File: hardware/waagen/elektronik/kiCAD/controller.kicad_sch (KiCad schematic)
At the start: 13 parts, among them J1 AVR-ISP-6, J2 Conn_01x06, U1 ATmega1284P-P, Y1 12MHz

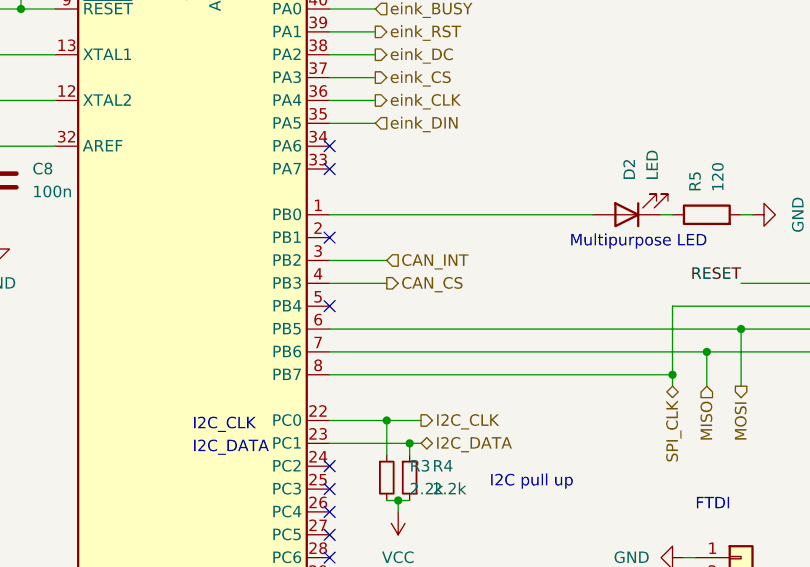
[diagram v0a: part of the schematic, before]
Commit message: CAN SPI CS pin corrected and PCB optimisations.
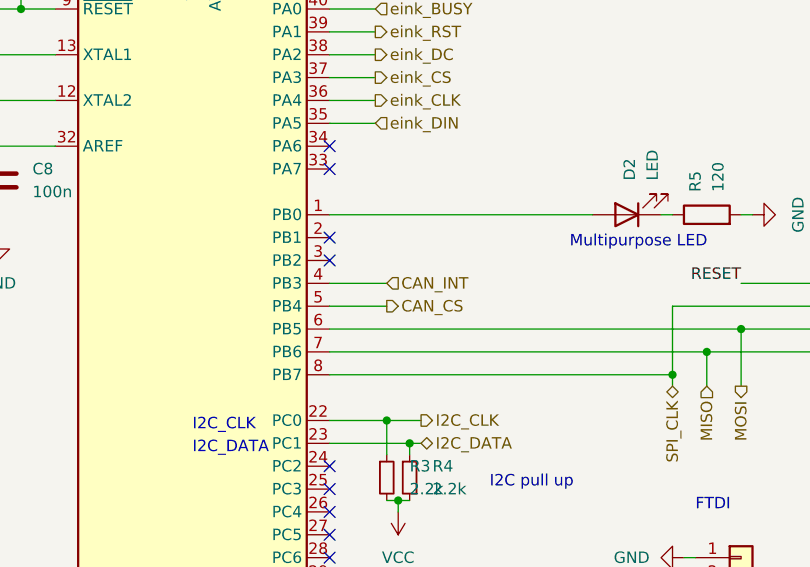
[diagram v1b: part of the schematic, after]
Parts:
- J1: footprint Connector_PinSocket_2.54mm:PinSocket_2x03_P2.54mm_Horizontal -> Connector_PinSocket_2.54mm:PinSocket_2x03_P2.54mm_Vertical
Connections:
- net CAN_CS: now also U1.5 (PB4); no longer U1.4 (PB3)
- net CAN_INT: now also U1.4 (PB3); no longer U1.3 (PB2)
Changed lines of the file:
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@@
   (no_connect (at 111.76 120.65))
   (no_connect (at 111.76 146.05))
-  (no_connect (at 111.76 95.25))
+  (no_connect (at 111.76 90.17))
   (no_connect (at 111.76 138.43))
   (no_connect (at 111.76 118.11))
@@
     (stroke (width 0) (type default) (color 0 0 0 0))
   )
-  (wire (pts (xy 111.76 90.17) (xy 118.11 90.17))
-    (stroke (width 0) (type default) (color 0 0 0 0))
-  )
   (wire (pts (xy 77.47 62.23) (xy 81.28 62.23))
     (stroke (width 0) (type default) (color 0 0 0 0))
@@
     (stroke (width 0) (type default) (color 0 0 0 0))
   )
+  (wire (pts (xy 111.76 95.25) (xy 118.11 95.25))
+    (stroke (width 0) (type default) (color 0 0 0 0))
+  )
   (wire (pts (xy 111.76 85.09) (xy 140.97 85.09))
     (stroke (width 0) (type default) (color 0 0 0 0))
   )
+  (wire (pts (xy 111.76 92.71) (xy 118.11 92.71))
+    (stroke (width 0) (type default) (color 0 0 0 0))
+  )
   (wire (pts (xy 148.59 85.09) (xy 149.86 85.09))
     (stroke (width 0) (type default) (color 0 0 0 0))
@@
   )
   (wire (pts (xy 157.48 92.71) (xy 166.37 92.71))
-    (stroke (width 0) (type default) (color 0 0 0 0))
-  )
-  (wire (pts (xy 111.76 92.71) (xy 118.11 92.71))
     (stroke (width 0) (type default) (color 0 0 0 0))
   )
@@
     (effects (font (size 1.27 1.27)) (justify right bottom))
   )
-  (hierarchical_label "CAN_INT" (shape input) (at 118.11 90.17 0)
+  (hierarchical_label "CAN_INT" (shape input) (at 118.11 92.71 0)
     (effects (font (size 1.27 1.27)) (justify left))
   )
@@
     (effects (font (size 1.27 1.27)) (justify left))
   )
-  (hierarchical_label "CAN_CS" (shape output) (at 118.11 92.71 0)
+  (hierarchical_label "CAN_CS" (shape output) (at 118.11 95.25 0)
     (effects (font (size 1.27 1.27)) (justify left))
   )
@@
       (effects (font (size 1.27 1.27)) (justify right))
     )
-    (property "Footprint" "Connector_PinSocket_2.54mm:PinSocket_2x03_P2.54mm_Horizontal" (id 2) (at 182.88 96.52 90)
-      (effects (font (size 1.27 1.27)) hide)
-    )
+    (property "Footprint" "Connector_PinSocket_2.54mm:PinSocket_2x03_P2.54mm_Vertical" (id 2) (at 182.88 96.52 90)
+      (effects (font (size 1.27 1.27)) hide)
+    )

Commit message: Error on JP1 fixed and changed scale wires pads
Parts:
- J2: footprint Connector_PinHeader_2.54mm:PinHeader_1x06_P2.54mm_Vertical -> Connector_PinSocket_2.54mm:PinSocket_1x06_P2.54mm_Vertical
- Y1: footprint Crystal:Crystal_SMD_HC49-SD -> Crystal:Crystal_SMD_HC49-SD_HandSoldering
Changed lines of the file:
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@@
       (effects (font (size 1.27 1.27)) (justify left))
     )
-    (property "Footprint" "Connector_PinHeader_2.54mm:PinHeader_1x06_P2.54mm_Vertical" (id 2) (at 157.48 128.27 0)
+    (property "Footprint" "Connector_PinSocket_2.54mm:PinSocket_1x06_P2.54mm_Vertical" (id 2) (at 157.48 128.27 0)
       (effects (font (size 1.27 1.27)) hide)
     )
@@
       (effects (font (size 1.27 1.27)) (justify right))
     )
-    (property "Footprint" "Crystal:Crystal_SMD_HC49-SD" (id 2) (at 60.96 71.12 0)
+    (property "Footprint" "Crystal:Crystal_SMD_HC49-SD_HandSoldering" (id 2) (at 60.96 71.12 0)
       (effects (font (size 1.27 1.27)) hide)
     )

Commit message: bus terminator and shelf controller added
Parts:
- J1: footprint Connector_PinSocket_2.54mm:PinSocket_2x03_P2.54mm_Vertical -> Connector_PinHeader_2.54mm:PinHeader_2x03_P2.54mm_Vertical
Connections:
- net VCC: no longer J1.2 (VCC), J2.3 (Pin_3)
- new net +9V: J1.2 (VCC), J2.3 (Pin_3)
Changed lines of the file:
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@@
     (stroke (width 0) (type default) (color 0 0 0 0))
   )
-  (wire (pts (xy 151.13 128.27) (xy 152.4 128.27))
+  (wire (pts (xy 148.59 128.27) (xy 152.4 128.27))
     (stroke (width 0) (type default) (color 0 0 0 0))
   )
@@
     (pin "1")
     (pin "2")
+  )
+  (symbol (lib_id "power:+9V") (at 179.07 110.49 180) (unit 1)
+    (in_bom yes) (on_board yes) (fields_autoplaced)
+    (property "Reference" "#PWR038" (id 0) (at 179.07 106.68 0)
+      (effects (font (size 1.27 1.27)) hide)
+    )
+    (property "Value" "+9V" (id 1) (at 179.07 115.57 0))
+    (property "Footprint" "" (id 2) (at 179.07 110.49 0)
+      (effects (font (size 1.27 1.27)) hide)
+    )
+    (property "Datasheet" "" (id 3) (at 179.07 110.49 0)
+      (effects (font (size 1.27 1.27)) hide)
+    )
+    (pin "1")
   )
   (symbol (lib_id "power:VCC") (at 119.38 118.11 180) (unit 1)
@@
     )
     (property "Datasheet" "" (id 3) (at 77.47 48.26 0)
-      (effects (font (size 1.27 1.27)) hide)
-    )
-    (pin "1")
-  )
-  (symbol (lib_id "power:VCC") (at 151.13 128.27 90) (unit 1)
-    (in_bom yes) (on_board yes) (fields_autoplaced)
-    (property "Reference" "#PWR020" (id 0) (at 154.94 128.27 0)
-      (effects (font (size 1.27 1.27)) hide)
-    )
-    (property "Value" "VCC" (id 1) (at 147.32 128.2699 90)
-      (effects (font (size 1.27 1.27)) (justify left))
-    )
-    (property "Footprint" "" (id 2) (at 151.13 128.27 0)
-      (effects (font (size 1.27 1.27)) hide)
-    )
-    (property "Datasheet" "" (id 3) (at 151.13 128.27 0)
       (effects (font (size 1.27 1.27)) hide)
     )
@@
       (effects (font (size 1.27 1.27)) (justify right))
     )
-    (property "Footprint" "Connector_PinSocket_2.54mm:PinSocket_2x03_P2.54mm_Vertical" (id 2) (at 182.88 96.52 90)
+    (property "Footprint" "Connector_PinHeader_2.54mm:PinHeader_2x03_P2.54mm_Vertical" (id 2) (at 182.88 96.52 90)
       (effects (font (size 1.27 1.27)) hide)
     )
@@
     (pin "6")
   )
-  (symbol (lib_id "power:VCC") (at 179.07 110.49 180) (unit 1)
-    (in_bom yes) (on_board yes) (fields_autoplaced)
-    (property "Reference" "#PWR038" (id 0) (at 179.07 106.68 0)
-      (effects (font (size 1.27 1.27)) hide)
-    )
-    (property "Value" "VCC" (id 1) (at 179.07 115.57 0))
-    (property "Footprint" "" (id 2) (at 179.07 110.49 0)
-      (effects (font (size 1.27 1.27)) hide)
-    )
-    (property "Datasheet" "" (id 3) (at 179.07 110.49 0)
-      (effects (font (size 1.27 1.27)) hide)
-    )
-    (pin "1")
-  )
   (symbol (lib_id "power:GND") (at 96.52 160.02 0) (unit 1)
     (in_bom yes) (on_board yes) (fields_autoplaced)
@@
       (effects (font (size 1.27 1.27)) hide)
     )
+    (pin "1")
+  )
+  (symbol (lib_id "power:+9V") (at 148.59 128.27 90) (unit 1)
+    (in_bom yes) (on_board yes)
+    (property "Reference" "#PWR020" (id 0) (at 152.4 128.27 0)
+      (effects (font (size 1.27 1.27)) hide)
+    )
+    (property "Value" "+9V" (id 1) (at 142.24 128.27 90)
+      (effects (font (size 1.27 1.27)) (justify right))
+    )
+    (property "Footprint" "" (id 2) (at 148.59 128.27 0)
+      (effects (font (size 1.27 1.27)) hide)
+    )
+    (property "Datasheet" "" (id 3) (at 148.59 128.27 0)
+      (effects (font (size 1.27 1.27)) hide)
+    )
